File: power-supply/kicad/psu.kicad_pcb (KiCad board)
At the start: 2 copper layers, 23 x 22.1 mm, 14 parts, among them J3 SSQ-103-03-G-D, U1 LM2776, U3 TPS72301DBVR, U5 TPS79333DBVR

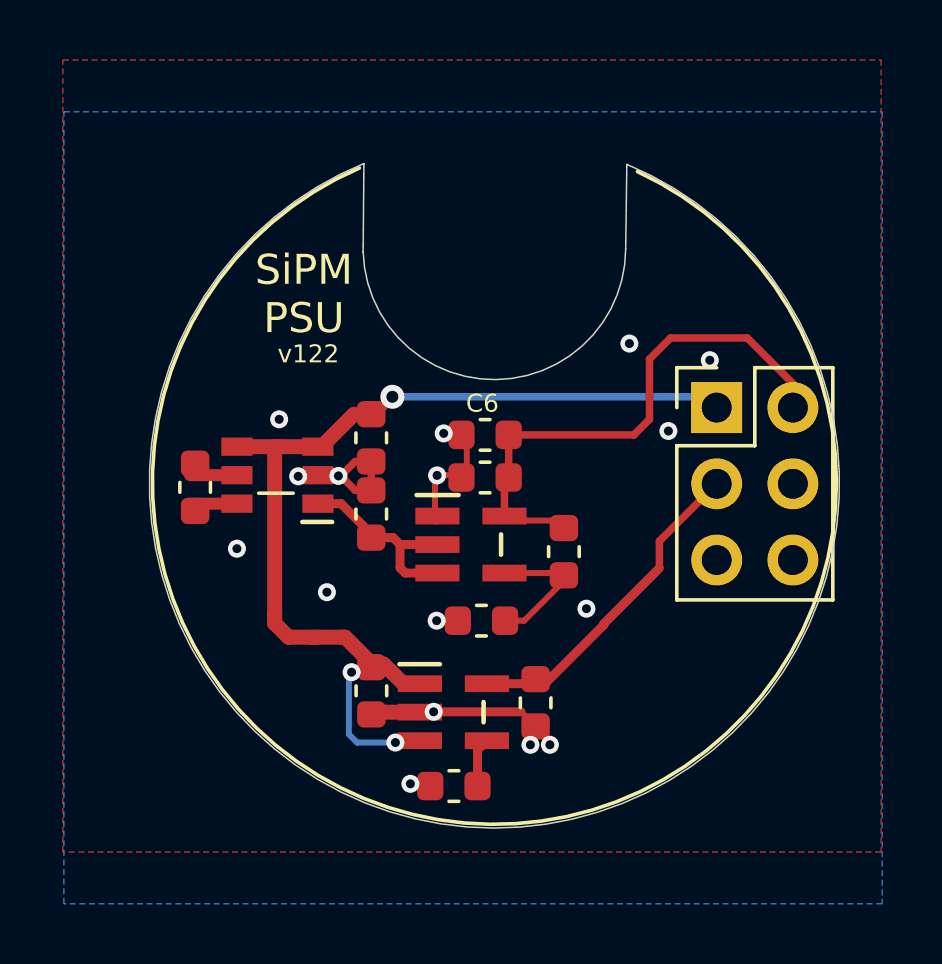
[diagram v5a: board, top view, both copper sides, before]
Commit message: Updated power supply to v122
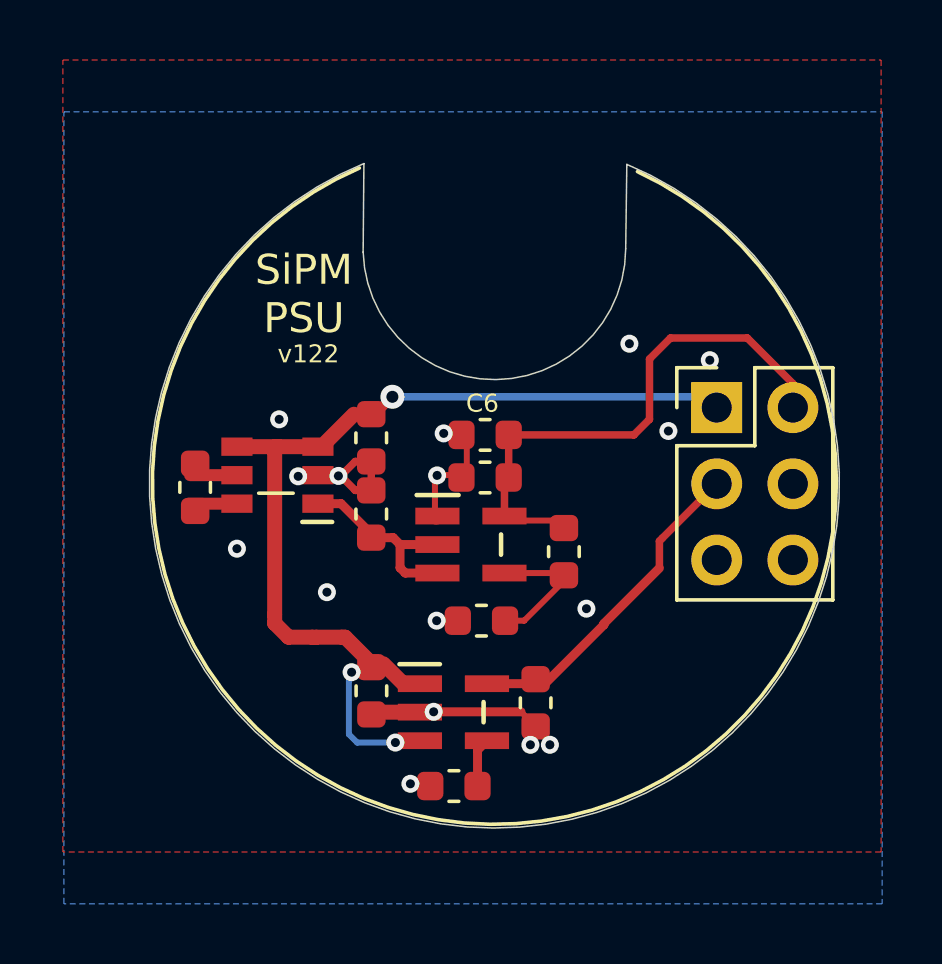
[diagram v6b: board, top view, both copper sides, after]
